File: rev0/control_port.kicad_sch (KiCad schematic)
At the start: 26 parts, among them IC1 ECP5-BGA256, U16 PI3USB102G, U8 USB3343-CP

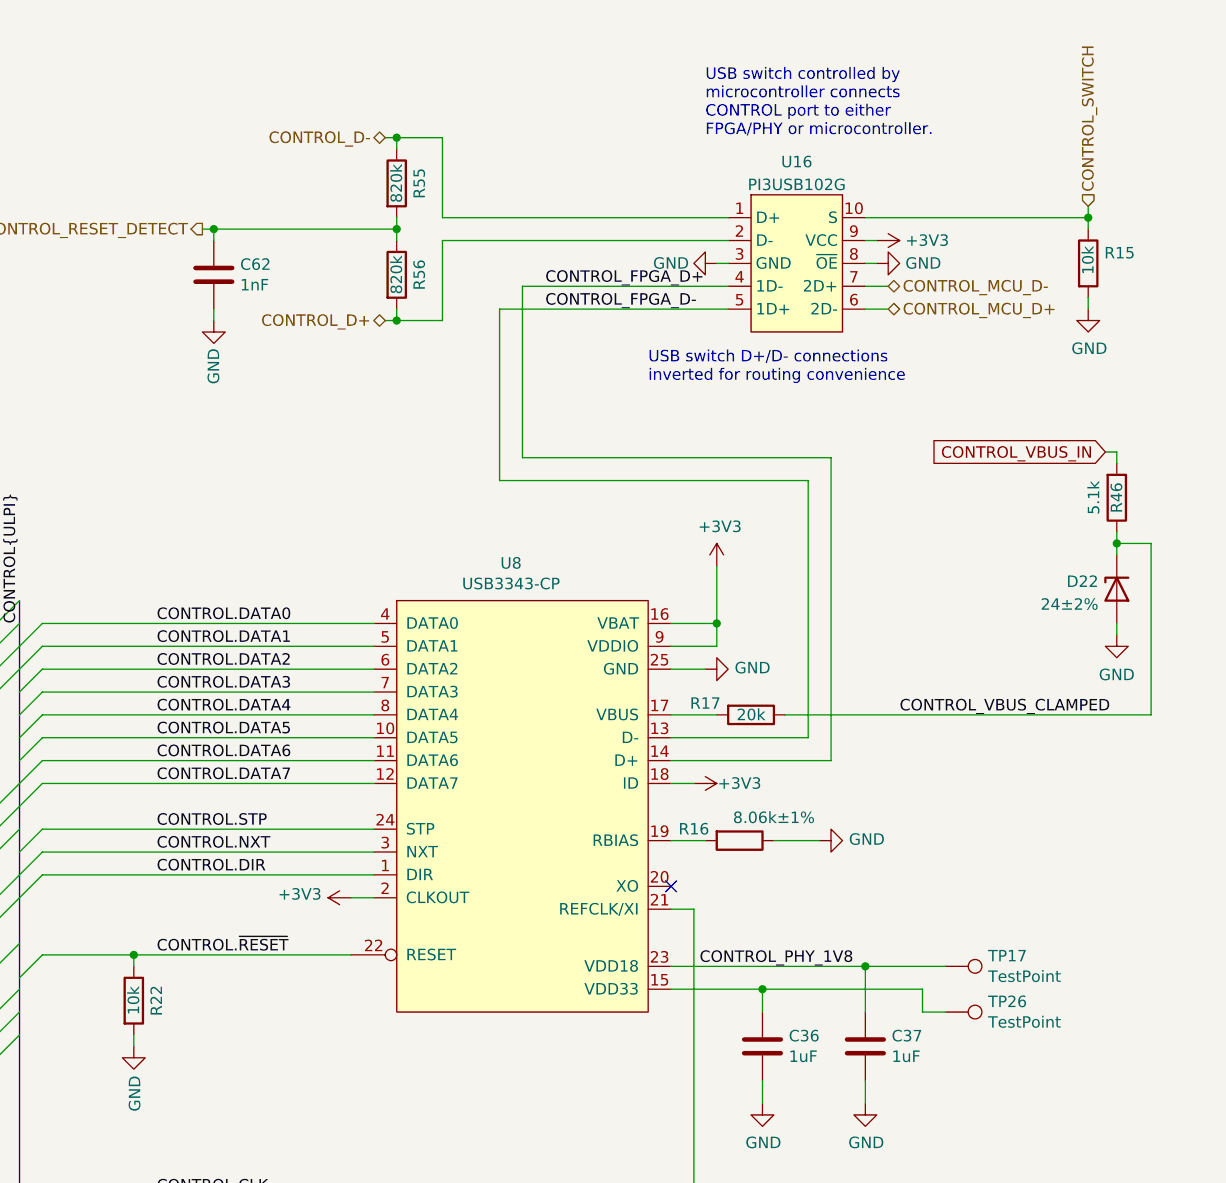
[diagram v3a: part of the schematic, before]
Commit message: hardware: update pull-up and pull-down resistors
- do not populate unnecessary resistors
- remove some unnecessary 0 ohm resistors
- add recommended FPGA resistors
- add recommended MCU resistors
- update hardware version detection pin strap
- change CONTROL port USB switch default to MCU
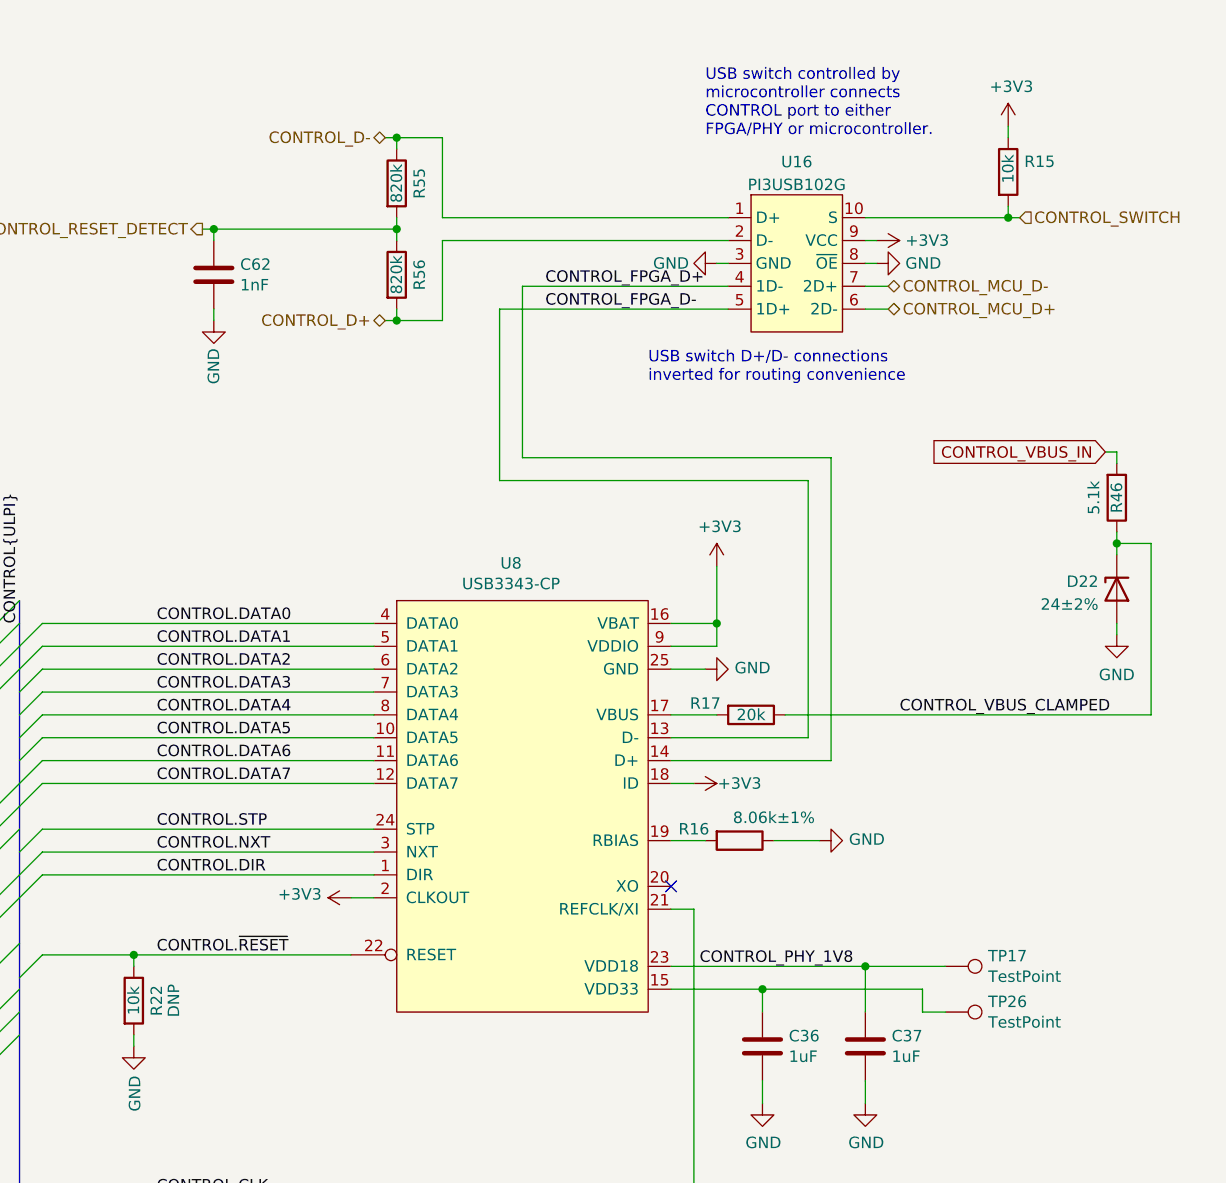
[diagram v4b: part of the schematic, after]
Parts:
- R22: DNP (none) -> DNP
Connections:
- net +3V3: now also R15.1
- net CONTROL_SWITCH: now also R15.2; no longer R15.1
- net GND: no longer R15.2
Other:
- moved on the sheet: R15
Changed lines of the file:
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@@
   (junction (at 63.5 34.29) (diameter 0) (color 0 0 0 0)
   )
-  (junction (at 272.415 41.275) (diameter 0) (color 0 0 0 0)
-  )
   (junction (at 152.4 175.26) (diameter 0) (color 0 0 0 0)
   )
@@
   )
   (junction (at 152.4 185.42) (diameter 0) (color 0 0 0 0)
+  )
+  (junction (at 263.525 41.275) (diameter 0) (color 0 0 0 0)
   )
   (junction (at 236.22 127) (diameter 0) (color 0 0 0 0)
@@
     (stroke (width 0) (type default) (color 0 0 0 0))
   )
-  (wire (pts (xy 272.415 41.275) (xy 272.415 42.545))
-    (stroke (width 0) (type default) (color 0 0 0 0))
-  )
   (wire (pts (xy 195.58 32.385) (xy 194.31 32.385))
     (stroke (width 0) (type default) (color 0 0 0 0))
@@
     (stroke (width 0) (type default) (color 0 0 0 0))
   )
+  (wire (pts (xy 263.525 31.115) (xy 263.525 32.385))
+    (stroke (width 0) (type default) (color 0 0 0 0))
+  )
   (wire (pts (xy 231.14 86.36) (xy 231.14 80.01))
     (stroke (width 0) (type default) (color 0 0 0 0))
@@
     (stroke (width 0) (type default) (color 0 0 0 0))
   )
+  (wire (pts (xy 263.525 41.275) (xy 247.65 41.275))
+    (stroke (width 0) (type default) (color 0 0 0 0))
+  )
   (wire (pts (xy 247.65 46.355) (xy 248.92 46.355))
     (stroke (width 0) (type default) (color 0 0 0 0))
@@
     (stroke (width 0) (type default) (color 0 0 0 0))
   )
-  (wire (pts (xy 272.415 41.275) (xy 247.65 41.275))
-    (stroke (width 0) (type default) (color 0 0 0 0))
-  )
   (wire (pts (xy 46.99 41.91) (xy 46.99 39.37))
     (stroke (width 0) (type default) (color 0 0 0 0))
@@
     (stroke (width 0) (type default) (color 0 0 0 0))
   )
-  (wire (pts (xy 272.415 41.275) (xy 272.415 40.005))
-    (stroke (width 0) (type default) (color 0 0 0 0))
-  )
   (wire (pts (xy 152.4 175.26) (xy 163.83 175.26))
     (stroke (width 0) (type default) (color 0 0 0 0))
@@
     (stroke (width 0) (type default) (color 0 0 0 0))
   )
+  (wire (pts (xy 263.525 41.275) (xy 264.795 41.275))
+    (stroke (width 0) (type default) (color 0 0 0 0))
+  )
   (wire (pts (xy 63.5 52.07) (xy 63.5 49.53))
     (stroke (width 0) (type default) (color 0 0 0 0))
@@
     (stroke (width 0) (type default) (color 0 0 0 0))
   )
+  (wire (pts (xy 263.525 40.005) (xy 263.525 41.275))
+    (stroke (width 0) (type default) (color 0 0 0 0))
+  )
   (wire (pts (xy 256.54 129.54) (xy 254 129.54))
-    (stroke (width 0) (type default) (color 0 0 0 0))
-  )
-  (wire (pts (xy 272.415 50.165) (xy 272.415 51.435))
     (stroke (width 0) (type default) (color 0 0 0 0))
   )
@@
     (effects (font (size 1.27 1.27)) (justify left))
   )
-  (hierarchical_label "CONTROL_SWITCH" (shape input) (at 272.415 40.005 90)
+  (hierarchical_label "CONTROL_SWITCH" (shape input) (at 264.795 41.275 0)
     (effects (font (size 1.27 1.27)) (justify left))
   )
@@
       (effects (font (size 1.27 1.27)) hide)
     )
+    (property "DNP" "DNP" (id 8) (at 170.815 128.27 90))
     (pin "1")
     (pin "2")
@@
     (pin "T9")
   )
+  (symbol (lib_id "power:+3V3") (at 263.525 31.115 0) (unit 1)
+    (in_bom yes) (on_board yes)
+    (property "Reference" "#PWR0149" (id 0) (at 263.525 34.925 0)
+      (effects (font (size 1.27 1.27)) hide)
+    )
+    (property "Value" "+3V3" (id 1) (at 263.8806 26.7208 0))
+    (property "Footprint" "" (id 2) (at 263.525 31.115 0)
+      (effects (font (size 1.27 1.27)) hide)
+    )
+    (property "Datasheet" "" (id 3) (at 263.525 31.115 0)
+      (effects (font (size 1.27 1.27)) hide)
+    )
+    (pin "1")
+  )
   (symbol (lib_id "power:GND") (at 175.26 52.705 0) (unit 1)
     (in_bom yes) (on_board yes)
@@
     (pin "1")
   )
-  (symbol (lib_id "power:GND") (at 272.415 51.435 0) (unit 1)
-    (in_bom yes) (on_board yes)
-    (property "Reference" "#PWR0149" (id 0) (at 272.415 57.785 0)
-      (effects (font (size 1.27 1.27)) hide)
-    )
-    (property "Value" "GND" (id 1) (at 272.542 55.8292 0))
-    (property "Footprint" "" (id 2) (at 272.415 51.435 0)
-      (effects (font (size 1.27 1.27)) hide)
-    )
-    (property "Datasheet" "" (id 3) (at 272.415 51.435 0)
-      (effects (font (size 1.27 1.27)) hide)
-    )
-    (pin "1")
-  )
   (symbol (lib_id "Device:C") (at 111.76 69.85 0) (unit 1)
     (in_bom yes) (on_board yes)
@@
     (pin "1")
   )
-  (symbol (lib_id "Device:R") (at 272.415 46.355 0) (unit 1)
-    (in_bom yes) (on_board yes)
-    (property "Reference" "R15" (id 0) (at 274.193 45.212 0)
-      (effects (font (size 1.27 1.27)) (justify left))
-    )
-    (property "Value" "10k" (id 1) (at 272.415 47.625 90)
-      (effects (font (size 1.27 1.27)) (justify left))
-    )
-    (property "Footprint" "Resistor_SMD:R_0402_1005Metric" (id 2) (at 270.637 46.355 90)
-      (effects (font (size 1.27 1.27)) hide)
-    )
-    (property "Datasheet" "~" (id 3) (at 272.415 46.355 0)
-      (effects (font (size 1.27 1.27)) hide)
-    )
-    (property "Part Number" "RC0402JR-0710KL" (id 4) (at 272.415 46.355 0)
-      (effects (font (size 1.27 1.27)) hide)
-    )
-    (property "Substitution" "any equivalent" (id 5) (at 272.415 46.355 0)
-      (effects (font (size 1.27 1.27)) hide)
-    )
-    (property "Description" "RES 10K OHM 5% 1/16W 0402" (id 6) (at 272.415 46.355 0)
-      (effects (font (size 1.27 1.27)) hide)
-    )
-    (property "Manufacturer" "Yageo" (id 7) (at 272.415 46.355 0)
-      (effects (font (size 1.27 1.27)) hide)
-    )
+  (symbol (lib_id "Device:R") (at 263.525 36.195 0) (unit 1)
+    (in_bom yes) (on_board yes)
+    (property "Reference" "R15" (id 0) (at 265.303 35.052 0)
+      (effects (font (size 1.27 1.27)) (justify left))
+    )
+    (property "Value" "10k" (id 1) (at 263.525 37.465 90)
+      (effects (font (size 1.27 1.27)) (justify left))
+    )
+    (property "Footprint" "Resistor_SMD:R_0402_1005Metric" (id 2) (at 261.747 36.195 90)
+      (effects (font (size 1.27 1.27)) hide)
+    )
+    (property "Datasheet" "~" (id 3) (at 263.525 36.195 0)
+      (effects (font (size 1.27 1.27)) hide)
+    )
+    (property "Part Number" "RC0402JR-0710KL" (id 4) (at 263.525 36.195 0)
+      (effects (font (size 1.27 1.27)) hide)
+    )
+    (property "Substitution" "any equivalent" (id 5) (at 263.525 36.195 0)
+      (effects (font (size 1.27 1.27)) hide)
+    )
+    (property "Description" "RES 10K OHM 5% 1/16W 0402" (id 6) (at 263.525 36.195 0)
+      (effects (font (size 1.27 1.27)) hide)
+    )
+    (property "Manufacturer" "Yageo" (id 7) (at 263.525 36.195 0)
+      (effects (font (size 1.27 1.27)) hide)
+    )

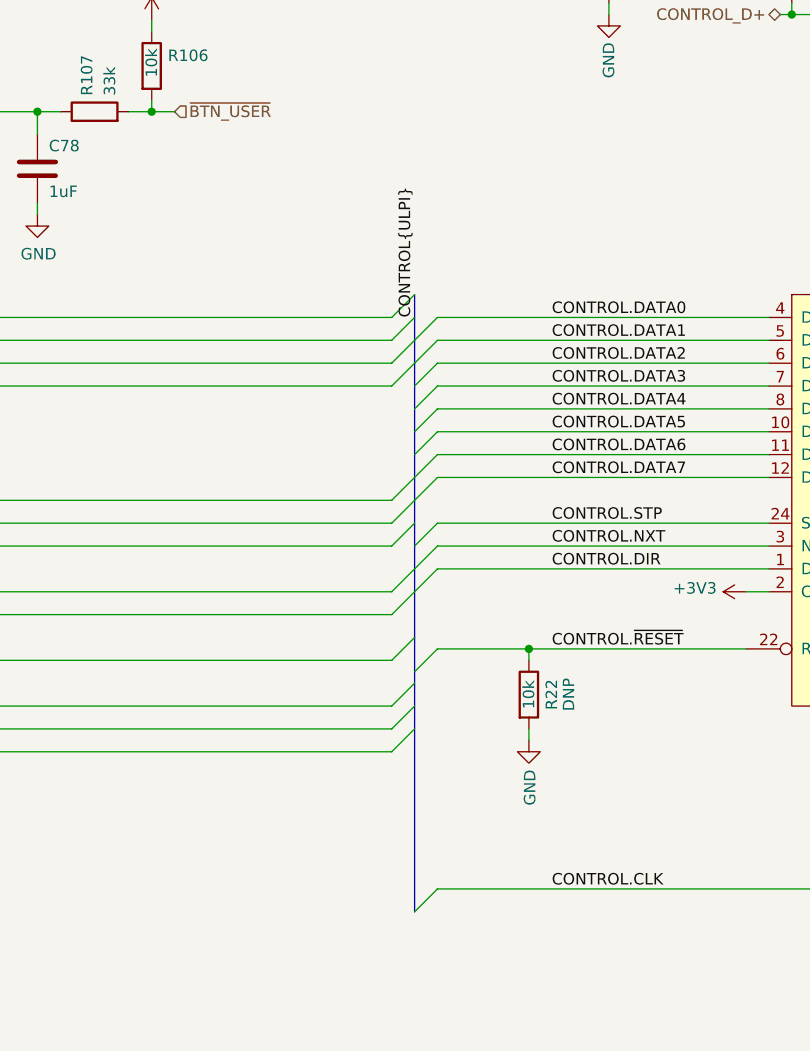
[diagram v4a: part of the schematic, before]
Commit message: hardware: clean up schematic for readability
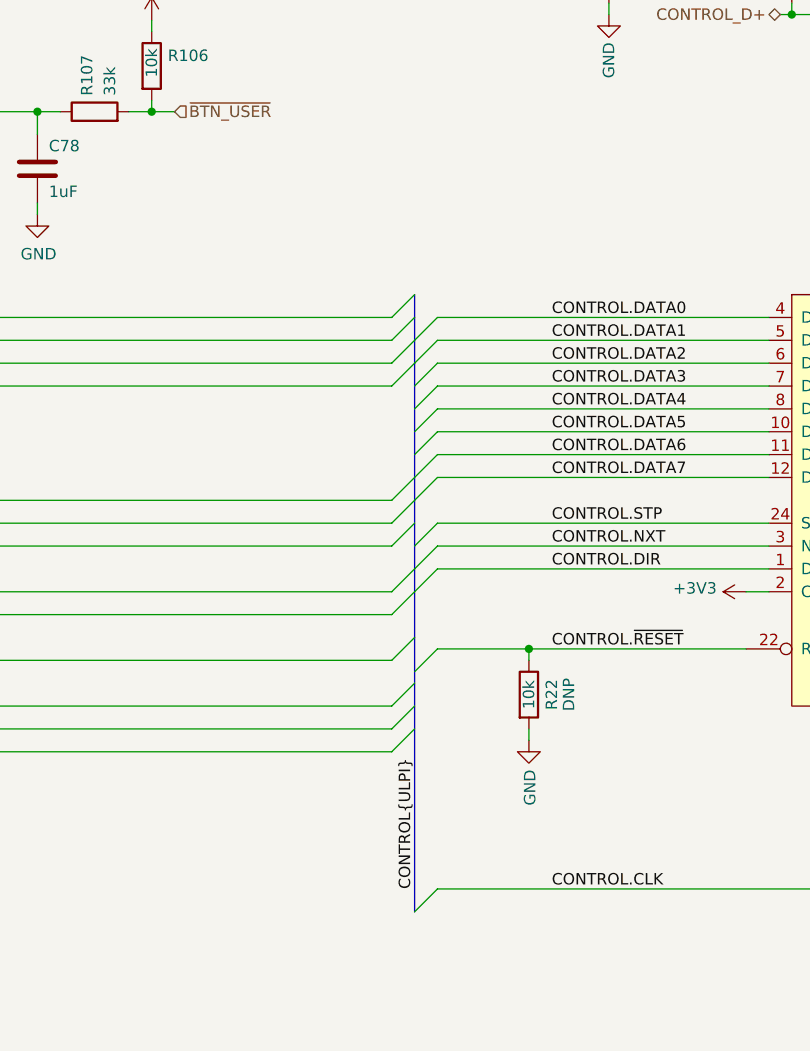
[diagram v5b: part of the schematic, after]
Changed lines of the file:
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@@
     (effects (font (size 1.27 1.27)) (justify left bottom))
   )
-  (label "CONTROL{ULPI}" (at 153.67 86.36 90)
+  (label "CONTROL{ULPI}" (at 153.67 149.86 90)
     (effects (font (size 1.27 1.27)) (justify left bottom))
   )
